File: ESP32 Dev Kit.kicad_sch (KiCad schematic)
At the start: 7 parts, among them U2 AMS1117-3.3

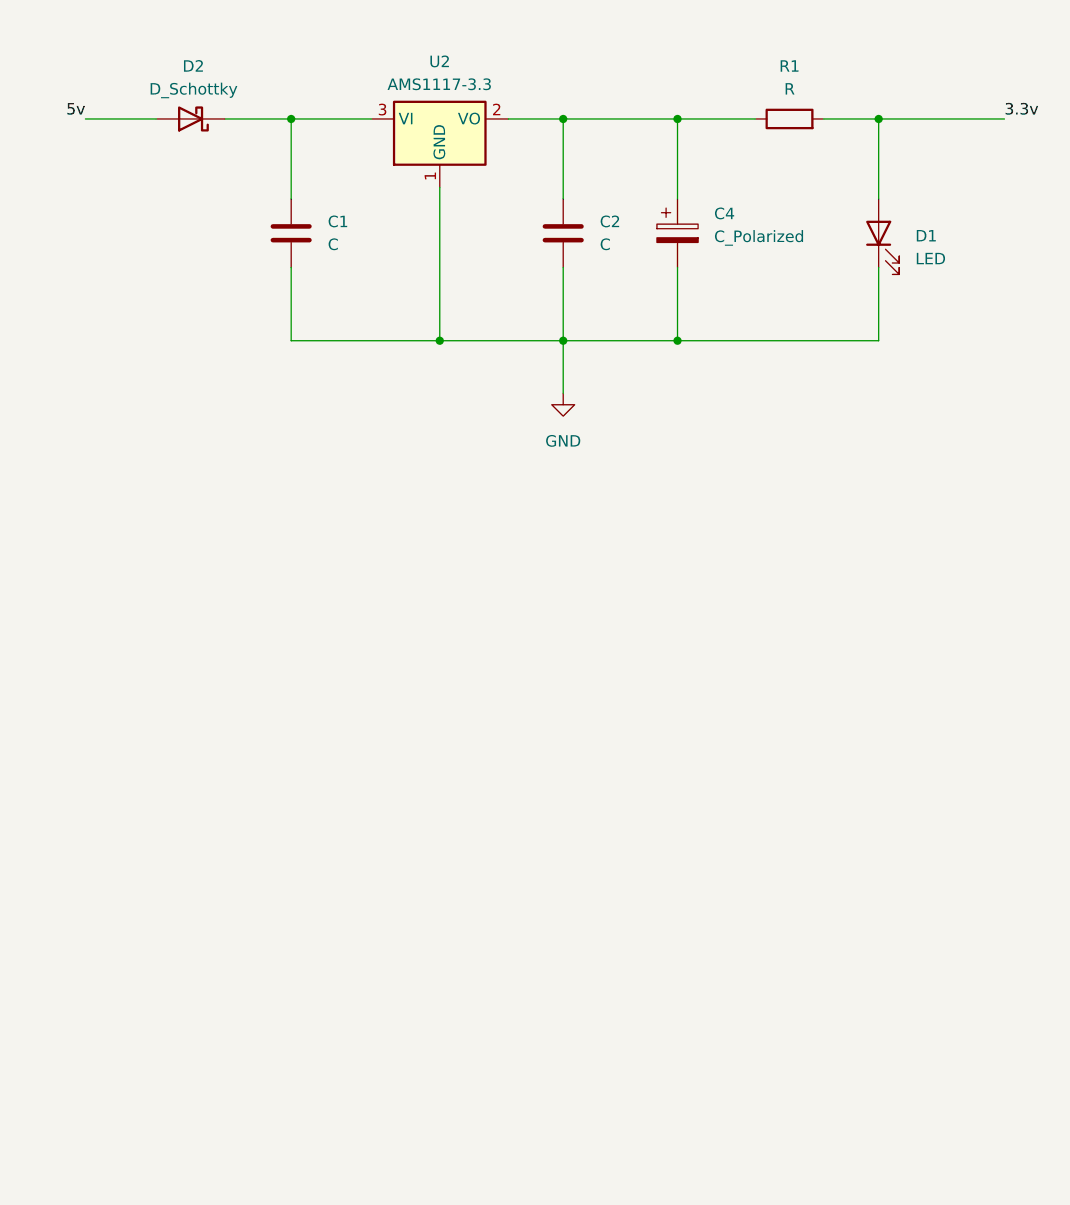
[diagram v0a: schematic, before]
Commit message: Added USB to UART Section
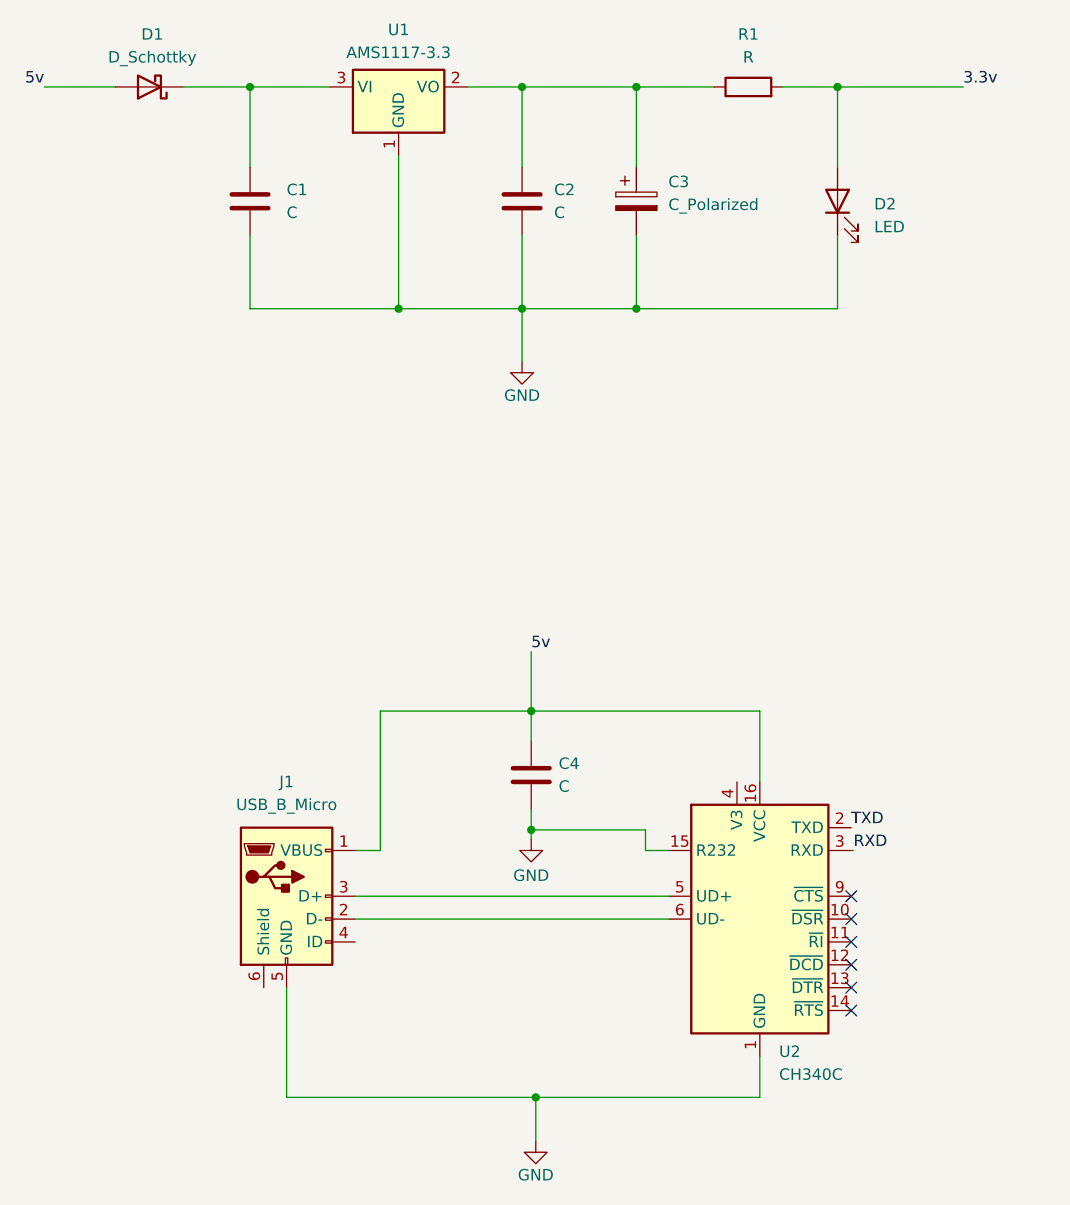
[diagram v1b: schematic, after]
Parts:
- added C4: C, symbol Device:C
- added J1: USB_B_Micro, symbol Connector:USB_B_Micro
- added U2: CH340C, SparkFun-Semiconductor-Standard:SO-16, symbol SparkFun-IC-Comm:CH340C
- renumbered C4 to C3, D2 to D1, D1 to D2, U2 to U1
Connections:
- net GND: now also C4.2, J1.5 (GND), U2.1 (GND), U2.15 (R232)
- new net: C4.1, J1.1 (VBUS), U2.16 (VCC)
- new net: J1.2 (D-), U2.6 (UD-)
- new net: J1.3 (D+), U2.5 (UD+)
- new net RXD: U2.3 (RXD)
- new net TXD: U2.2 (TXD)
- no-connect marks 0 -> 6
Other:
- moved on the sheet: C1, C2, C3, D1, D2, R1, U1

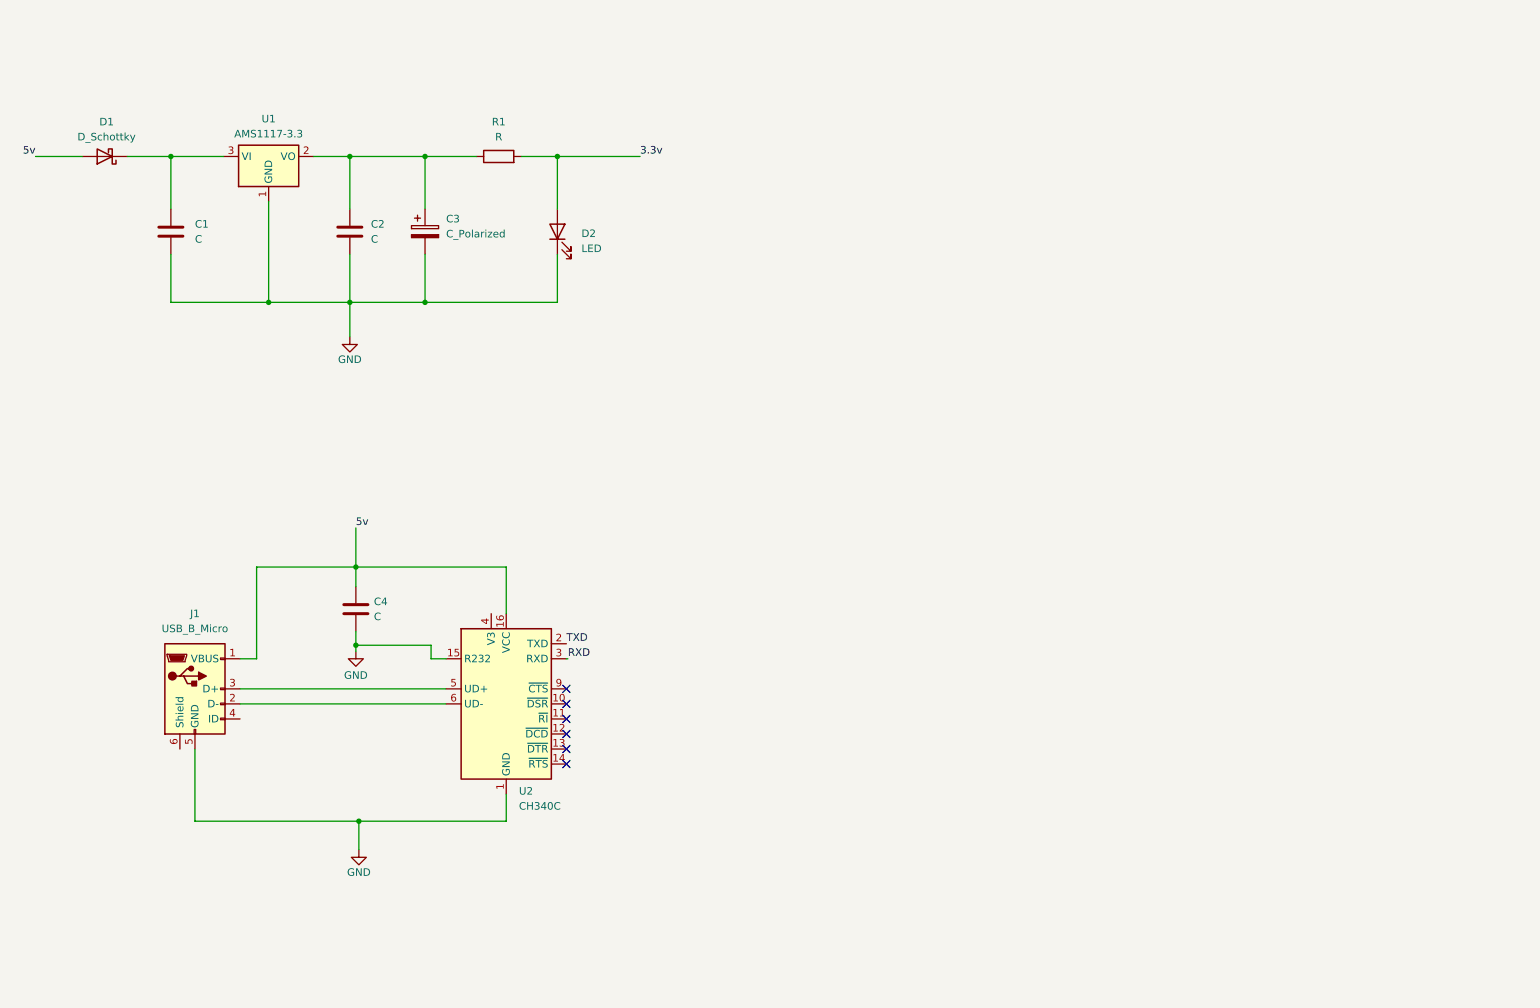
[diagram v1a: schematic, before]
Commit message: ESP32 Chip and Auto Reset/Boot Sections Added
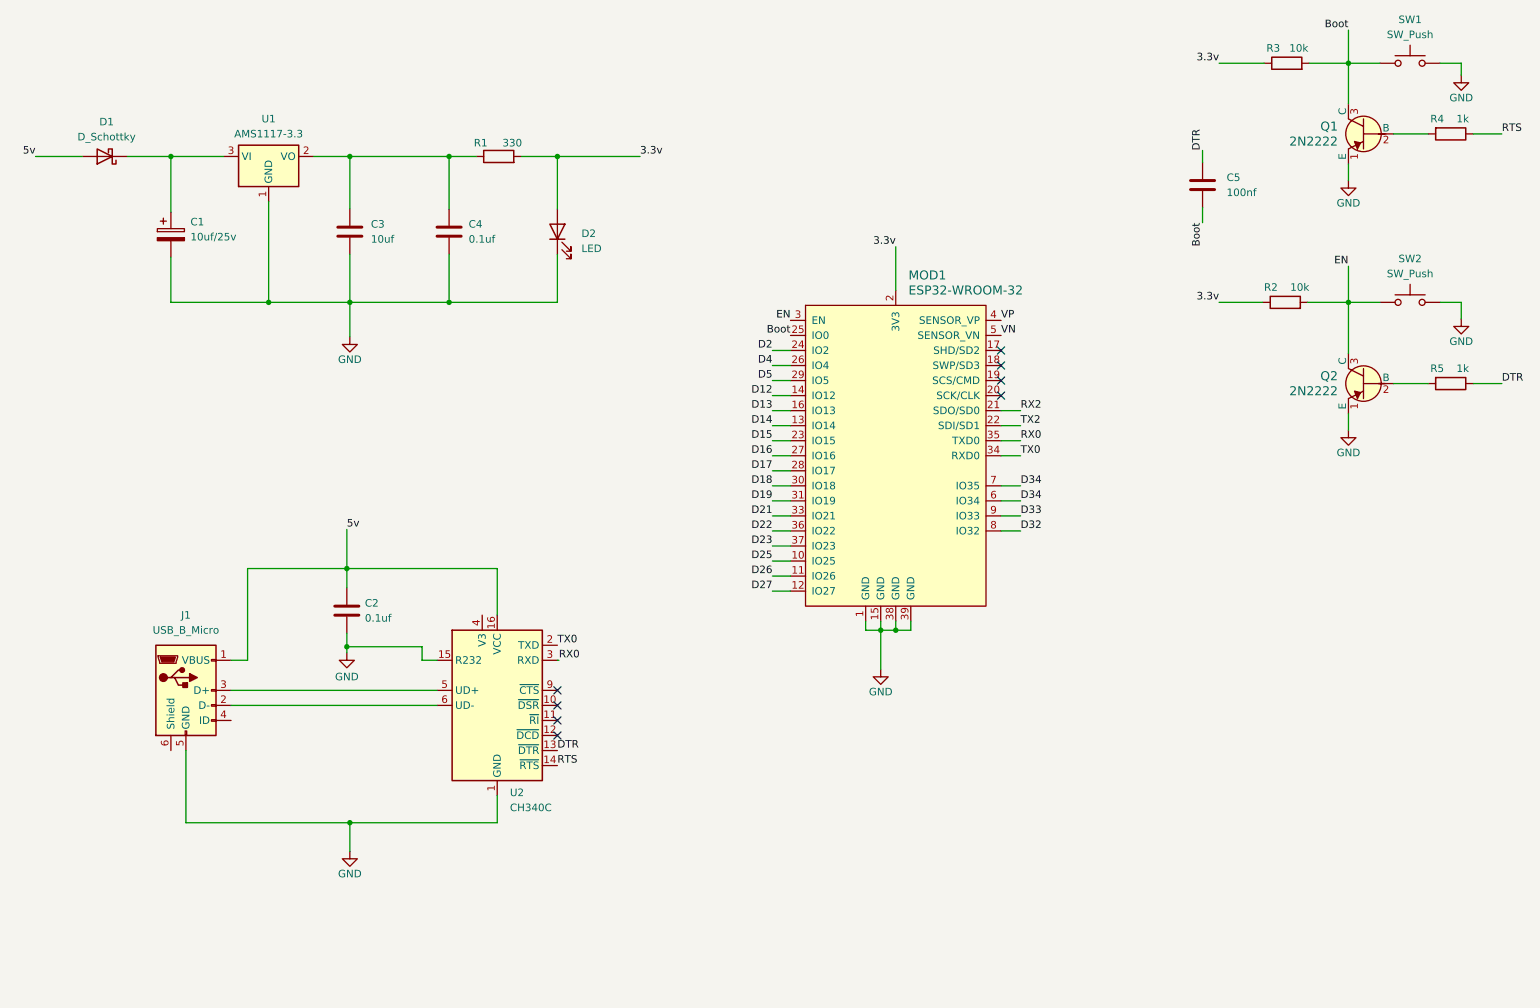
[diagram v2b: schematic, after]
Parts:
- added C5: 100nf, symbol Device:C
- added MOD1: ESP32-WROOM-32, digikey-footprints:ESP32-WROOM-32D, symbol dk_RF-Transceiver-Modules:ESP32-WROOM-32
- added Q1, Q2: 2N2222, digikey-footprints:TO-18-3, symbol dk_Transistors-Bipolar-BJT-Single:2N2222
- added R2, R3: 10k, symbol Device:R
- added R4, R5: 1k, symbol Device:R
- added SW1, SW2: SW_Push, symbol Switch:SW_Push
- C1: renamed from C3; value C_Polarized -> 10uf/25v
- C2: renamed from C4; value C -> 0.1uf
- C3: renamed from C2; value C -> 10uf
- C4: renamed from C1; value C -> 0.1uf
- R1: value R -> 330
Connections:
- net 3.3v: now also MOD1.2 (3V3), R2.1, R3.1
- net GND: now also MOD1.1 (GND), MOD1.15 (GND), MOD1.38 (GND), MOD1.39 (GND), Q1.1 (E), Q2.1 (E), SW1.2, SW2.2
- net at C3.1, R1.1, U1.2 (VO): now also C4.1; no longer C1.1
- net at D1.1 (K), U1.3 (VI): now also C1.1; no longer C4.1
- net DTR: now reaches U2.13 (~{DTR})
- net DTR: now also C5.1, R5.1
- net RTS: now reaches U2.14 (~{RTS})
- net RTS: now also R4.1
- net RXD renamed RX0
- net RX0: now also MOD1.35 (TXD0)
- net TXD renamed TX0
- net TX0: now also MOD1.34 (RXD0)
- new net: Q2.2 (B), R5.2
- new net: Q1.2 (B), R4.2
- new net Boot: C5.2, MOD1.25 (IO0), Q1.3 (C), R3.2, SW1.1
- new net D12: MOD1.14 (IO12)
- new net D13: MOD1.16 (IO13)
- new net D14: MOD1.13 (IO14)
- new net D15: MOD1.23 (IO15)
- new net D16: MOD1.27 (IO16)
- new net D17: MOD1.28 (IO17)
- new net D18: MOD1.30 (IO18)
- new net D19: MOD1.31 (IO19)
- new net D2: MOD1.24 (IO2)
- new net D21: MOD1.33 (IO21)
- new net D22: MOD1.36 (IO22)
- new net D23: MOD1.37 (IO23)
- new net D25: MOD1.10 (IO25)
- new net D26: MOD1.11 (IO26)
- new net D27: MOD1.12 (IO27)
- new net D32: MOD1.8 (IO32)
- new net D33: MOD1.9 (IO33)
- new net D34: MOD1.6 (IO34), MOD1.7 (IO35)
- new net D4: MOD1.26 (IO4)
- new net D5: MOD1.29 (IO5)
- new net EN: MOD1.3 (EN), Q2.3 (C), R2.2, SW2.1
- new net RX2: MOD1.21 (SDO/SD0)
- new net TX2: MOD1.22 (SDI/SD1)
- new net VN: MOD1.5 (SENSOR_VN)
- new net VP: MOD1.4 (SENSOR_VP)
- no-connect marks 6 -> 8
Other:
- title: ESP32 Dev Kit V1 (30 pin) -> ESP32 Dev Kit V1 (30 pin) Clone
- moved on the sheet: C1, C2, C4, J1, U2

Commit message: Added Jumpers Section
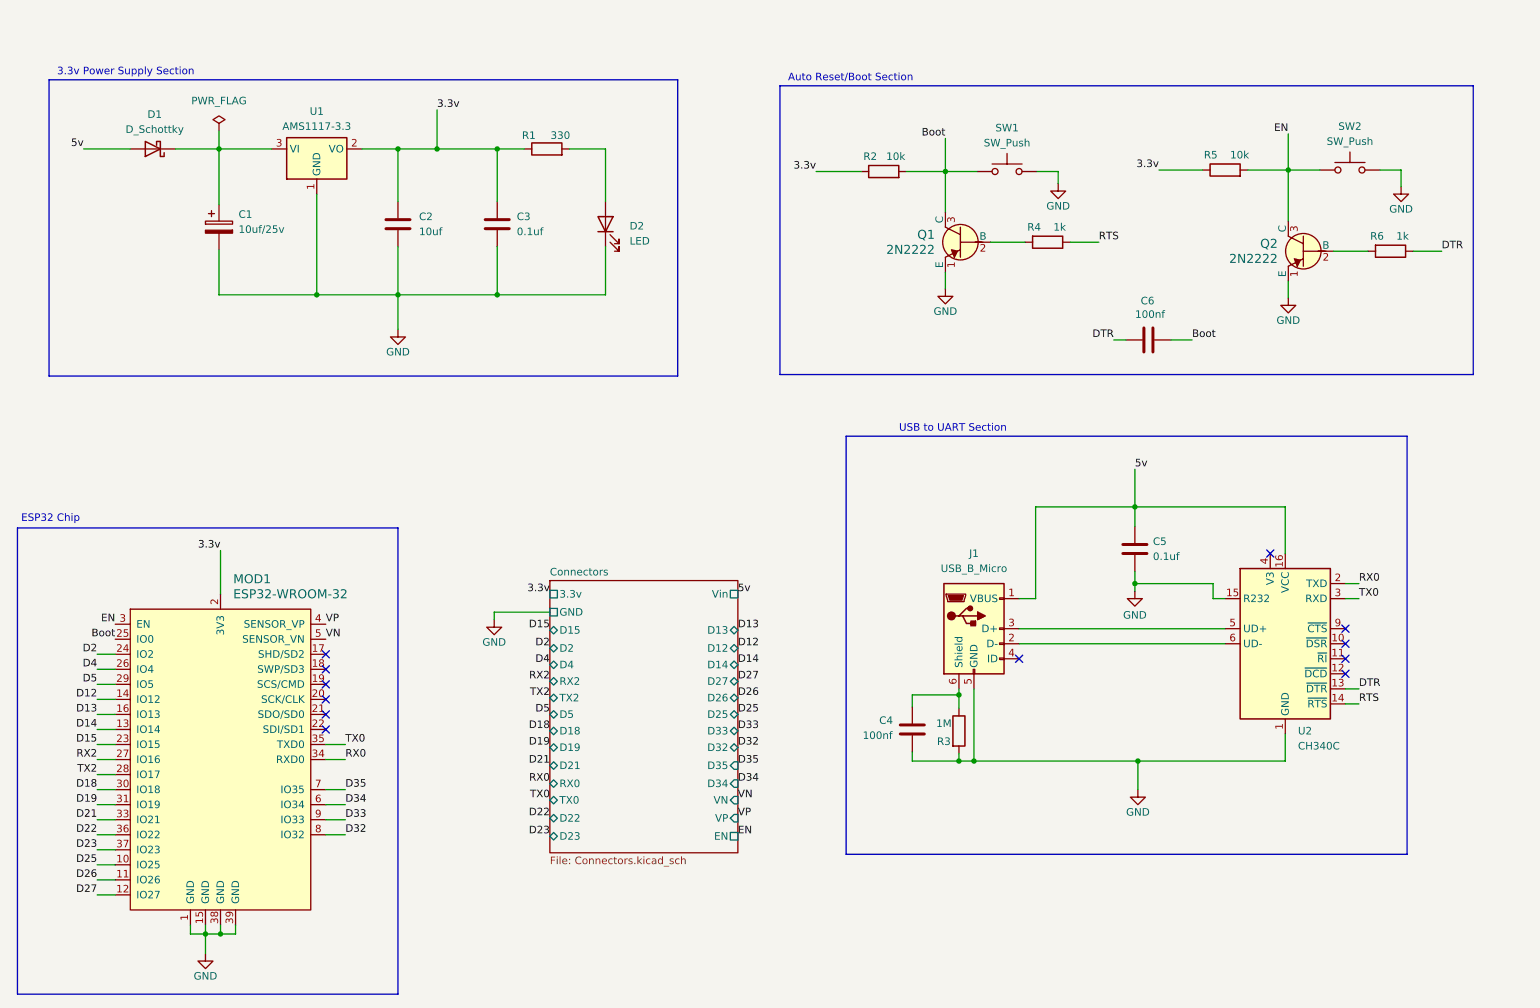
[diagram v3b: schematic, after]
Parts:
- added C4: 100nf, symbol Device:C
- added R3: 1M, symbol Device:R
- renumbered C3 to C2, C4 to C3, C2 to C5, C5 to C6, R3 to R2, R2 to R5, R5 to R6
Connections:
- net D16 is gone; now on net RX2: MOD1.27 (IO16)
- net D17 is gone; now on net TX2: MOD1.28 (IO17)
- net 3.3v: now also C2.1, C3.1, R1.1, U1.2 (VO); no longer D2.2 (A), R1.2
- net 5v: now also C5.1, J1.1 (VBUS), U2.16 (VCC)
- net D34: no longer MOD1.7 (IO35)
- net GND: now also C4.2, R3.2
- net RX0: now also MOD1.34 (RXD0), U2.2 (TXD); no longer MOD1.35 (TXD0), U2.3 (RXD)
- net RX2: no longer MOD1.21 (SDO/SD0)
- net TX0: now also MOD1.35 (TXD0), U2.3 (RXD); no longer MOD1.34 (RXD0), U2.2 (TXD)
- net TX2: no longer MOD1.22 (SDI/SD1)
- net at J1.6 (Shield): now also C4.1, R3.1
- new net: D2.2 (A), R1.2
- new net D35: MOD1.7 (IO35)
- no-connect marks 8 -> 12
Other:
- added sheet Connectors (Connectors.kicad_sch)
- note added: "3.3v Power Supply Section"
- note added: "Auto Reset/Boot Section"
- note added: "ESP32 Chip"
- note added: "USB to UART Section"
- moved on the sheet: C1, C2, C3, C5, C6, D1, D2, J1, MOD1, Q1, Q2, R1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
